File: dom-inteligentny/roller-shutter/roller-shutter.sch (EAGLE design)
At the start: 12 parts, among them K1 RP421110, K2 RP421110, Q1 16MHz, U1 ATMEGA328

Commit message: WIP
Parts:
- removed C3: 0.1uF, adafruit:C-USC0805
- added D1, D2: (no value), adafruit:DIODE_SOD-123FL
- added K3: 691218410003, Wurth_Elektronik_Electromechanic_Terminal_Blocks_Connectors_rev15c:691218410003
- added K4: RP421110, relay:RP421110
- added R2, R3: (no value), eagle-ltspice:RR1206
- added T1, T2: BC847, transistor:BC847
- C1: value 22pF -> (none); device adafruit:C-USC1206 -> rcl:CPOL-EUSANYO_SMD_C6
- C2: value 22pF -> 0.1uF; device adafruit:C-USC1206 -> adafruit:C-USC0805
- C4: value (none) -> 22pF; device rcl:CPOL-EUSANYO_SMD_C6 -> adafruit:C-USC1206
- C5: value 0.1uF -> 22pF; device adafruit:C-USC0805 -> adafruit:C-USC1206
- K2: value RP421110 -> 691218410003; device relay:RP421110 -> Wurth_Elektronik_Electromechanic_Terminal_Blocks_Connectors_rev15c:691218410003
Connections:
- new net N$1: D1.A, K11.1, T1.C
- new net N$2: D2.A, K41.1, T2.C
- new net N$4: K12.P, K13.P, K3.3, K42.P, K43.P
- new net N$5: R2.2, T1.B
- new net N$6: R3.2, T2.B
- new net N$7: K12.S, K13.S, K3.2
- new net N$8: K3.1, K42.S, K43.S
- net A0: now also R2.1
- net A1: now also R3.1
- net AREF: now also C6.1; no longer C5.1
- net GND: now also C1.-, C4.2, T1.E, T2.E; no longer C1.2, C3.2, C4.-
- net N$43: now also C4.1; no longer C2.1
- net N$44: now also C5.1; no longer C1.1
- net VCC: now also C1.+, C2.1, D1.C, D2.C, K41.2; no longer C3.1, C4.+, C6.1, K21.2
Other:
- moved on the sheet: C2, C5, C6

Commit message: Roller shutter
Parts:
- removed K2, K3: 691218410003, Wurth_Elektronik_Electromechanic_Terminal_Blocks_Connectors_rev15c:691218410003
- added C3, C7: (no value), eagle-ltspice:C
- added C8, C9: (no value), eagle-ltspice:CC1812
- added JP2: (no value), pinhead:PINHD-1X3
- added R4, R5: (no value), eagle-ltspice:RR1206
- added R6, R7: (no value), eagle-ltspice:RR2512
- added X1, X4: (no value), con-ptr500:AK500/3
- added X2, X3: JST-XH-05-PIN-LONG-PAD, Rembrandt Electronics - JST XH Connectors v1-0:JST-XH-05-PIN-LONG-PAD
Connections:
- new net N$10: C9.2, R6.1
- new net N$9: C8.2, R7.1
- net A2: now also C7.2, R5.1, X4-3.KL
- net A3: now also C3.2, R4.1, X4-2.KL
- net A4: now also X2-2.S, X3-2.S
- net A5: now also X2-1.S, X3-1.S
- net GND: now also C3.1, C7.1, X2-4.S, X2-5.S, X3-4.S, X3-5.S, X4-1.KL
- net N$1: now also JP2.1
- net N$2: now also JP2.2
- net N$4: now also C8.1, C9.1, X1-1.KL; no longer K3.3
- net N$7: now also R7.2, X1-3.KL; no longer K3.2
- net N$8: now also R6.2, X1-2.KL; no longer K3.1
- net VCC: now also JP2.3, R4.2, R5.2, X2-3.S, X3-3.S

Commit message: roller shutter
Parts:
- added JP6: (no value), pinhead-zmiany-JP:PINHD-3X4
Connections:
- net D10: now also JP6.2
- net D7: now also JP6.11
- net D8: now also JP6.8
- net D9: now also JP6.5
- net GND: now also JP6.12, JP6.3, JP6.6, JP6.9
- net VCC: now also JP6.1, JP6.10, JP6.4, JP6.7
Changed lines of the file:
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@@
 <part name="X4" library="con-ptr500" library_urn="urn:adsk.eagle:library:181" deviceset="AK500/3" device="" package3d_urn="urn:adsk.eagle:package:9883/1"/>
 <part name="X1" library="con-ptr500" library_urn="urn:adsk.eagle:library:181" deviceset="AK500/3" device="" package3d_urn="urn:adsk.eagle:package:9883/1"/>
+<part name="GND9" library="supply1" library_urn="urn:adsk.eagle:library:371" deviceset="GND" device=""/>
+<part name="P+8" library="supply1" library_urn="urn:adsk.eagle:library:371" deviceset="VCC" device=""/>
+<part name="JP6" library="pinhead-zmiany-JP" deviceset="PINHD-3X4" device=""/>
 </parts>
 <sheets>
@@
 <attribute name="VALUE" x="308.483" y="39.37" size="1.778" layer="96" rot="R90"/>
 </instance>
+<instance part="GND9" gate="1" x="358.14" y="119.38" smashed="yes">
+<attribute name="VALUE" x="355.6" y="116.84" size="1.778" layer="96"/>
+</instance>
+<instance part="P+8" gate="VCC" x="342.9" y="177.8" smashed="yes">
+<attribute name="VALUE" x="340.36" y="175.26" size="1.778" layer="96" rot="R90"/>
+</instance>
+<instance part="JP6" gate="G$1" x="345.44" y="160.02" smashed="yes">
+<attribute name="NAME" x="339.09" y="168.275" size="1.778" layer="95"/>
+<attribute name="VALUE" x="339.09" y="152.4" size="1.778" layer="96"/>
+</instance>
 </instances>
 <busses>
@@
 <label x="259.08" y="147.32" size="1.778" layer="95" xref="yes"/>
 </segment>
+<segment>
+<pinref part="JP6" gate="G$1" pin="11"/>
+<wire x1="350.52" y1="157.48" x2="353.06" y2="157.48" width="0.1524" layer="91"/>
+<wire x1="353.06" y1="157.48" x2="353.06" y2="149.86" width="0.1524" layer="91"/>
+<wire x1="353.06" y1="149.86" x2="340.36" y2="149.86" width="0.1524" layer="91"/>
+<label x="340.36" y="149.86" size="1.778" layer="95" rot="R180" xref="yes"/>
+</segment>
 </net>
 <net name="D8" class="0">
@@
 <label x="248.92" y="142.24" size="1.778" layer="95" xref="yes"/>
 </segment>
+<segment>
+<pinref part="JP6" gate="G$1" pin="8"/>
+<wire x1="350.52" y1="160.02" x2="355.6" y2="160.02" width="0.1524" layer="91"/>
+<wire x1="355.6" y1="160.02" x2="355.6" y2="149.86" width="0.1524" layer="91"/>
+<label x="355.6" y="149.86" size="1.778" layer="95" rot="R270" xref="yes"/>
+</segment>
 </net>
 <net name="D9" class="0">
@@
 <label x="259.08" y="139.7" size="1.778" layer="95" xref="yes"/>
 </segment>
+<segment>
+<pinref part="JP6" gate="G$1" pin="5"/>
+<wire x1="355.6" y1="172.72" x2="355.6" y2="162.56" width="0.1524" layer="91"/>
+<wire x1="355.6" y1="162.56" x2="350.52" y2="162.56" width="0.1524" layer="91"/>
+<label x="355.6" y="172.72" size="1.778" layer="95" xref="yes"/>
+</segment>
 </net>
 <net name="D10" class="0">
@@
 <wire x1="238.76" y1="137.16" x2="248.92" y2="137.16" width="0.1524" layer="91"/>
 <label x="248.92" y="137.16" size="1.778" layer="95" xref="yes"/>
+</segment>
+<segment>
+<pinref part="JP6" gate="G$1" pin="2"/>
+<wire x1="353.06" y1="170.18" x2="353.06" y2="165.1" width="0.1524" layer="91"/>
+<wire x1="353.06" y1="165.1" x2="350.52" y2="165.1" width="0.1524" layer="91"/>
+<label x="353.06" y="170.18" size="1.778" layer="95" rot="R90" xref="yes"/>
 </segment>
 </net>
@@
 <wire x1="325.12" y1="187.96" x2="325.12" y2="185.42" width="0.1524" layer="91"/>
 </segment>
+<segment>
+<pinref part="GND9" gate="1" pin="GND"/>
+<pinref part="JP6" gate="G$1" pin="3"/>
+<pinref part="JP6" gate="G$1" pin="6"/>
+<wire x1="358.14" y1="165.1" x2="358.14" y2="162.56" width="0.1524" layer="91"/>
+<pinref part="JP6" gate="G$1" pin="9"/>
+<wire x1="358.14" y1="162.56" x2="358.14" y2="160.02" width="0.1524" layer="91"/>
+<junction x="358.14" y="162.56"/>
+<pinref part="JP6" gate="G$1" pin="12"/>
+<wire x1="358.14" y1="160.02" x2="358.14" y2="157.48" width="0.1524" layer="91"/>
+<junction x="358.14" y="160.02"/>
+<wire x1="358.14" y1="157.48" x2="358.14" y2="121.92" width="0.1524" layer="91"/>
+<junction x="358.14" y="157.48"/>
+</segment>
 </net>
 <net name="VCC" class="0">
@@
 <label x="350.52" y="91.44" size="1.778" layer="95" rot="R90" xref="yes"/>
 </segment>
-</net>
+<segment>
+<pinref part="P+8" gate="VCC" pin="VCC"/>
+<pinref part="JP6" gate="G$1" pin="1"/>
+<wire x1="342.9" y1="175.26" x2="342.9" y2="165.1" width="0.1524" layer="91"/>
+<pinref part="JP6" gate="G$1" pin="4"/>
+<wire x1="342.9" y1="165.1" x2="342.9" y2="162.56" width="0.1524" layer="91"/>
+<junction x="342.9" y="165.1"/>
+<pinref part="JP6" gate="G$1" pin="7"/>
+<wire x1="342.9" y1="162.56" x2="342.9" y2="160.02" width="0.1524" layer="91"/>
+<junction x="342.9" y="162.56"/>
+<pinref part="JP6" gate="G$1" pin="10"/>
+<wire x1="342.9" y1="160.02" x2="342.9" y2="157.48" width="0.1524" layer="91"/>
+<junction x="342.9" y="160.02"/>
+</segment>
+</net>

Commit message: Roller shutter ark change
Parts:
- removed X1: (no value), con-ptr500:AK500/3
- added X5: (no value), con-ptr500:AK500/4
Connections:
- new net N$11: C8.1, C9.1, X5-2.KL
- net N$4: now also X5-1.KL; no longer C8.1, C9.1, X1-1.KL
- net N$7: now also X5-4.KL; no longer X1-3.KL
- net N$8: now also X5-3.KL; no longer X1-2.KL
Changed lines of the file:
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@@
 <part name="JP2" library="pinhead" library_urn="urn:adsk.eagle:library:325" deviceset="PINHD-1X3" device="" package3d_urn="urn:adsk.eagle:package:22458/2"/>
 <part name="X4" library="con-ptr500" library_urn="urn:adsk.eagle:library:181" deviceset="AK500/3" device="" package3d_urn="urn:adsk.eagle:package:9883/1"/>
-<part name="X1" library="con-ptr500" library_urn="urn:adsk.eagle:library:181" deviceset="AK500/3" device="" package3d_urn="urn:adsk.eagle:package:9883/1"/>
 <part name="GND9" library="supply1" library_urn="urn:adsk.eagle:library:371" deviceset="GND" device=""/>
 <part name="P+8" library="supply1" library_urn="urn:adsk.eagle:library:371" deviceset="VCC" device=""/>
 <part name="JP6" library="pinhead-zmiany-JP" deviceset="PINHD-3X4" device=""/>
+<part name="X5" library="con-ptr500" library_urn="urn:adsk.eagle:library:181" deviceset="AK500/4" device="" package3d_urn="urn:adsk.eagle:package:9887/1"/>
 </parts>
 <sheets>
@@
 <attribute name="VALUE" x="334.01" y="171.577" size="1.778" layer="96" rot="MR0"/>
 </instance>
-<instance part="X1" gate="-1" x="294.64" y="43.18" smashed="yes" rot="R90">
-<attribute name="NAME" x="293.751" y="41.91" size="1.778" layer="95" rot="R270"/>
-</instance>
-<instance part="X1" gate="-2" x="299.72" y="43.18" smashed="yes" rot="R90">
-<attribute name="NAME" x="298.831" y="41.91" size="1.778" layer="95" rot="R270"/>
-</instance>
-<instance part="X1" gate="-3" x="304.8" y="43.18" smashed="yes" rot="R90">
-<attribute name="NAME" x="303.911" y="41.91" size="1.778" layer="95" rot="R270"/>
-<attribute name="VALUE" x="308.483" y="39.37" size="1.778" layer="96" rot="R90"/>
-</instance>
 <instance part="GND9" gate="1" x="358.14" y="119.38" smashed="yes">
 <attribute name="VALUE" x="355.6" y="116.84" size="1.778" layer="96"/>
@@
 <attribute name="NAME" x="339.09" y="168.275" size="1.778" layer="95"/>
 <attribute name="VALUE" x="339.09" y="152.4" size="1.778" layer="96"/>
+</instance>
+<instance part="X5" gate="-1" x="294.64" y="43.18" smashed="yes" rot="R90">
+<attribute name="NAME" x="293.751" y="41.91" size="1.778" layer="95" rot="R270"/>
+</instance>
+<instance part="X5" gate="-2" x="299.72" y="43.18" smashed="yes" rot="R90">
+<attribute name="NAME" x="298.831" y="41.91" size="1.778" layer="95" rot="R270"/>
+</instance>
+<instance part="X5" gate="-3" x="304.8" y="43.18" smashed="yes" rot="R90">
+<attribute name="NAME" x="303.911" y="41.91" size="1.778" layer="95" rot="R270"/>
+</instance>
+<instance part="X5" gate="-4" x="309.88" y="43.18" smashed="yes" rot="R90">
+<attribute name="NAME" x="308.991" y="41.91" size="1.778" layer="95" rot="R270"/>
+<attribute name="VALUE" x="313.563" y="39.37" size="1.778" layer="96" rot="R90"/>
 </instance>
 </instances>
@@
 <pinref part="K1" gate="3" pin="P"/>
 <wire x1="279.4" y1="68.58" x2="264.16" y2="68.58" width="0.1524" layer="91"/>
-<wire x1="309.88" y1="68.58" x2="307.34" y2="68.58" width="0.1524" layer="91"/>
 <junction x="309.88" y="68.58"/>
 <junction x="279.4" y="68.58"/>
-<wire x1="307.34" y1="68.58" x2="279.4" y2="68.58" width="0.1524" layer="91"/>
+<wire x1="309.88" y1="68.58" x2="279.4" y2="68.58" width="0.1524" layer="91"/>
 <wire x1="264.16" y1="68.58" x2="264.16" y2="58.42" width="0.1524" layer="91"/>
 <junction x="264.16" y="68.58"/>
 <wire x1="264.16" y1="58.42" x2="294.64" y2="58.42" width="0.1524" layer="91"/>
-<pinref part="C8" gate="G$1" pin="1"/>
-<wire x1="251.46" y1="55.88" x2="251.46" y2="53.34" width="0.1524" layer="91"/>
-<wire x1="251.46" y1="53.34" x2="264.16" y2="53.34" width="0.1524" layer="91"/>
-<wire x1="264.16" y1="53.34" x2="264.16" y2="58.42" width="0.1524" layer="91"/>
-<junction x="264.16" y="58.42"/>
-<pinref part="C9" gate="G$1" pin="1"/>
-<wire x1="345.44" y1="55.88" x2="345.44" y2="53.34" width="0.1524" layer="91"/>
-<wire x1="345.44" y1="53.34" x2="307.34" y2="53.34" width="0.1524" layer="91"/>
-<wire x1="307.34" y1="53.34" x2="307.34" y2="68.58" width="0.1524" layer="91"/>
-<junction x="307.34" y="68.58"/>
-<pinref part="X1" gate="-1" pin="KL"/>
+<wire x1="309.88" y1="55.88" x2="309.88" y2="68.58" width="0.1524" layer="91"/>
+<junction x="309.88" y="68.58"/>
 <wire x1="294.64" y1="48.26" x2="294.64" y2="58.42" width="0.1524" layer="91"/>
+<pinref part="X5" gate="-1" pin="KL"/>
 </segment>
 </net>
@@
 <junction x="287.02" y="73.66"/>
 <wire x1="299.72" y1="73.66" x2="299.72" y2="53.34" width="0.1524" layer="91"/>
+<wire x1="299.72" y1="53.34" x2="309.88" y2="53.34" width="0.1524" layer="91"/>
+<pinref part="X5" gate="-4" pin="KL"/>
+<wire x1="309.88" y1="53.34" x2="309.88" y2="48.26" width="0.1524" layer="91"/>
 <pinref part="R7" gate="G$1" pin="2"/>
-<wire x1="251.46" y1="73.66" x2="271.78" y2="73.66" width="0.1524" layer="91"/>
+<wire x1="271.78" y1="73.66" x2="251.46" y2="73.66" width="0.1524" layer="91"/>
 <junction x="271.78" y="73.66"/>
-<wire x1="299.72" y1="53.34" x2="304.8" y2="53.34" width="0.1524" layer="91"/>
-<pinref part="X1" gate="-3" pin="KL"/>
-<wire x1="304.8" y1="53.34" x2="304.8" y2="48.26" width="0.1524" layer="91"/>
 </segment>
 </net>
@@
 <junction x="317.5" y="73.66"/>
 <wire x1="302.26" y1="73.66" x2="302.26" y2="50.8" width="0.1524" layer="91"/>
+<wire x1="302.26" y1="50.8" x2="304.8" y2="50.8" width="0.1524" layer="91"/>
+<pinref part="X5" gate="-3" pin="KL"/>
+<wire x1="304.8" y1="50.8" x2="304.8" y2="48.26" width="0.1524" layer="91"/>
 <pinref part="R6" gate="G$1" pin="2"/>
-<wire x1="332.74" y1="73.66" x2="345.44" y2="73.66" width="0.1524" layer="91"/>
+<wire x1="345.44" y1="73.66" x2="332.74" y2="73.66" width="0.1524" layer="91"/>
 <junction x="332.74" y="73.66"/>
-<wire x1="302.26" y1="50.8" x2="299.72" y2="50.8" width="0.1524" layer="91"/>
-<pinref part="X1" gate="-2" pin="KL"/>
-<wire x1="299.72" y1="50.8" x2="299.72" y2="48.26" width="0.1524" layer="91"/>
 </segment>
 </net>
@@
 </segment>
 </net>
+<net name="N$11" class="0">
+<segment>
+<pinref part="C8" gate="G$1" pin="1"/>
+<wire x1="251.46" y1="55.88" x2="251.46" y2="50.8" width="0.1524" layer="91"/>
+<pinref part="X5" gate="-2" pin="KL"/>
+<wire x1="299.72" y1="48.26" x2="299.72" y2="50.8" width="0.1524" layer="91"/>
+<wire x1="299.72" y1="50.8" x2="284.48" y2="50.8" width="0.1524" layer="91"/>
+<wire x1="284.48" y1="50.8" x2="284.48" y2="33.02" width="0.1524" layer="91"/>
+<wire x1="284.48" y1="33.02" x2="320.04" y2="33.02" width="0.1524" layer="91"/>
+<wire x1="320.04" y1="33.02" x2="320.04" y2="50.8" width="0.1524" layer="91"/>
+<wire x1="251.46" y1="50.8" x2="284.48" y2="50.8" width="0.1524" layer="91"/>
+<junction x="284.48" y="50.8"/>
+<wire x1="320.04" y1="50.8" x2="345.44" y2="50.8" width="0.1524" layer="91"/>
+<pinref part="C9" gate="G$1" pin="1"/>
+<wire x1="345.44" y1="50.8" x2="345.44" y2="55.88" width="0.1524" layer="91"/>
+</segment>
+</net>

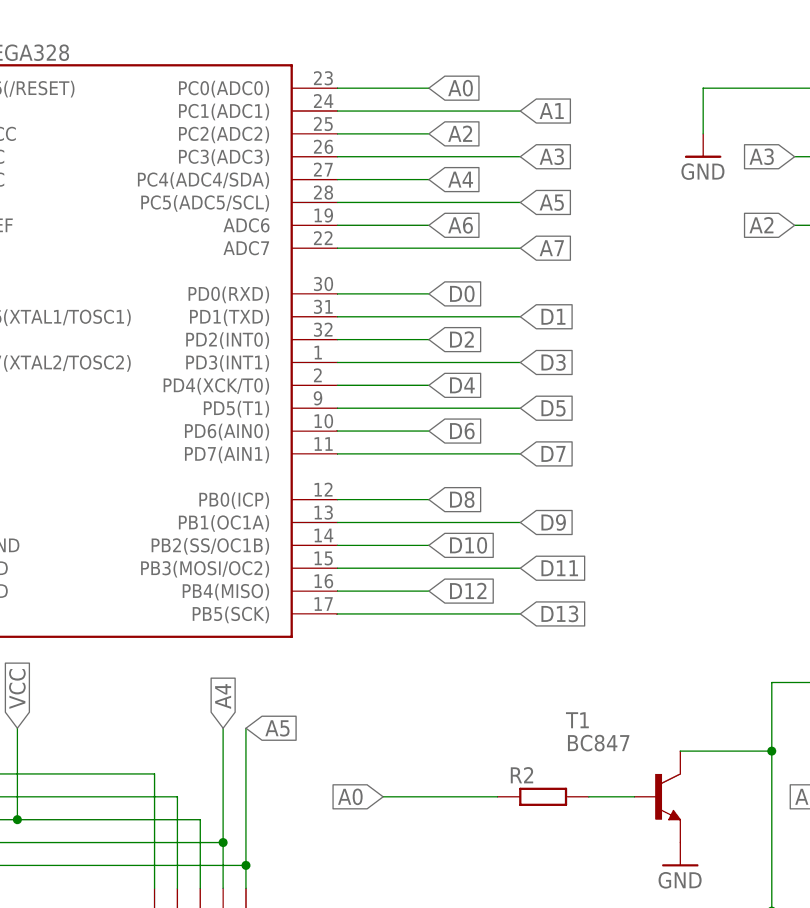
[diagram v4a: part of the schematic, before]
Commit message: Roller shutter, heat controller WIP and a new light switch input board
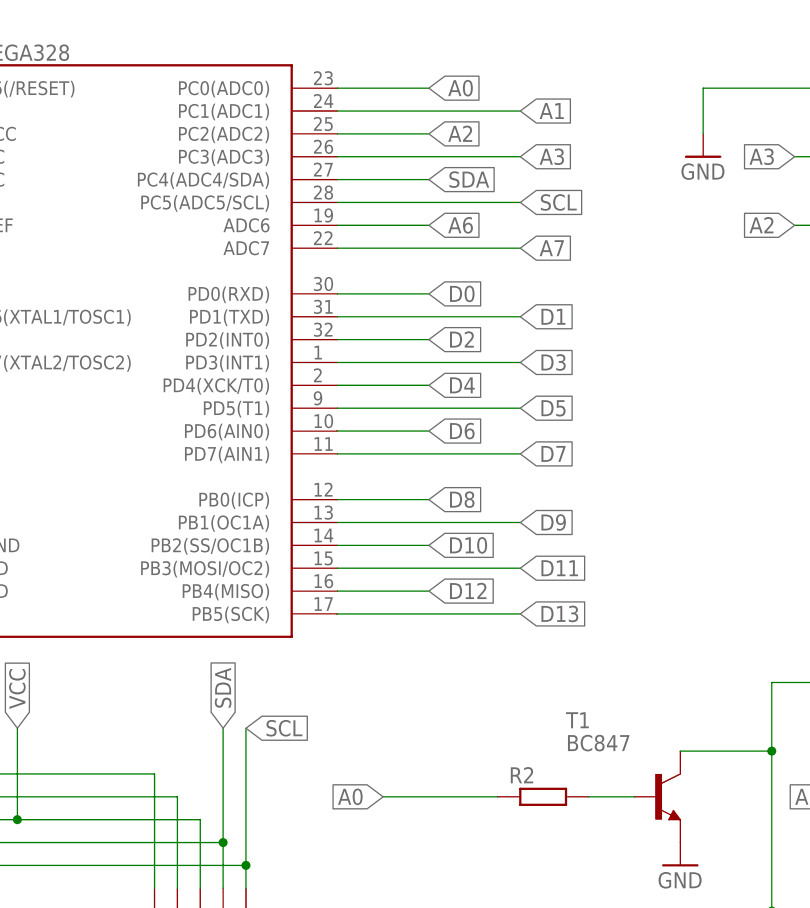
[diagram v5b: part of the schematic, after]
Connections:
- net A4 renamed SDA
- net A5 renamed SCL
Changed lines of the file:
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@@
 </segment>
 </net>
-<net name="A4" class="0">
+<net name="SDA" class="0">
 <segment>
 <pinref part="U1" gate="G$1" pin="PC4(ADC4/SDA)"/>
@@
 <junction x="226.06" y="104.14"/>
 <label x="226.06" y="116.84" size="1.778" layer="95" rot="R90" xref="yes"/>
-</segment>
-</net>
-<net name="A5" class="0">
-<segment>
-<pinref part="U1" gate="G$1" pin="PC5(ADC5/SCL)"/>
-<wire x1="238.76" y1="175.26" x2="259.08" y2="175.26" width="0.1524" layer="91"/>
-<label x="259.08" y="175.26" size="1.778" layer="95" xref="yes"/>
-</segment>
-<segment>
-<pinref part="X3" gate="-1" pin="S"/>
-<wire x1="193.04" y1="99.06" x2="193.04" y2="101.6" width="0.1524" layer="91"/>
-<wire x1="193.04" y1="101.6" x2="228.6" y2="101.6" width="0.1524" layer="91"/>
-<pinref part="X2" gate="-1" pin="S"/>
-<wire x1="228.6" y1="101.6" x2="228.6" y2="99.06" width="0.1524" layer="91"/>
-<wire x1="228.6" y1="101.6" x2="228.6" y2="116.84" width="0.1524" layer="91"/>
-<junction x="228.6" y="101.6"/>
-<label x="228.6" y="116.84" size="1.778" layer="95" xref="yes"/>
 </segment>
 </net>
@@
 </segment>
 </net>
+<net name="SCL" class="0">
+<segment>
+<pinref part="U1" gate="G$1" pin="PC5(ADC5/SCL)"/>
+<wire x1="238.76" y1="175.26" x2="259.08" y2="175.26" width="0.1524" layer="91"/>
+<label x="259.08" y="175.26" size="1.778" layer="95" xref="yes"/>
+</segment>
+<segment>
+<pinref part="X3" gate="-1" pin="S"/>
+<wire x1="193.04" y1="99.06" x2="193.04" y2="101.6" width="0.1524" layer="91"/>
+<wire x1="193.04" y1="101.6" x2="228.6" y2="101.6" width="0.1524" layer="91"/>
+<pinref part="X2" gate="-1" pin="S"/>
+<wire x1="228.6" y1="101.6" x2="228.6" y2="99.06" width="0.1524" layer="91"/>
+<wire x1="228.6" y1="101.6" x2="228.6" y2="116.84" width="0.1524" layer="91"/>
+<junction x="228.6" y="101.6"/>
+<label x="228.6" y="116.84" size="1.778" layer="95" xref="yes"/>
+</segment>
+</net>
